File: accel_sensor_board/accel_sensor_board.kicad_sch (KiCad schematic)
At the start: 31 parts, among them J1 TagConnect_TC2030-NL, J2 USB_C_Receptacle_USB2.0_16P, SW1 SW_Push, U1 STM32F405RGT6, U2 USBLC6-2SC6, U3 TXB0106PW, U4 DIX9211PTR, X1 16MHz, X2 32kHz768

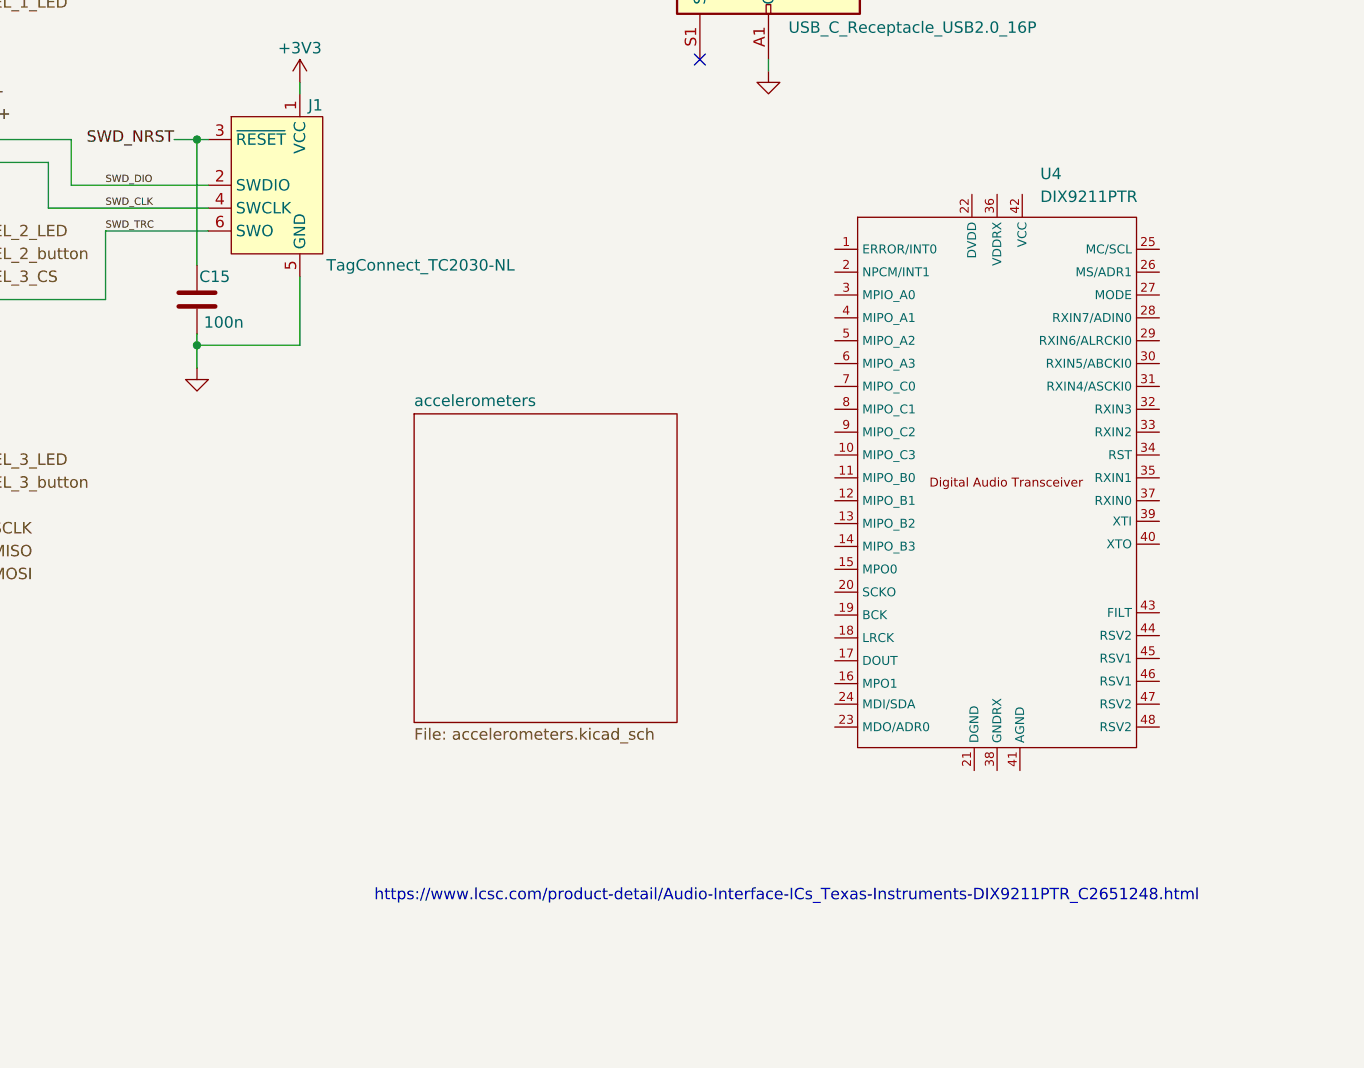
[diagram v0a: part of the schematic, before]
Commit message: added different audio driver / dac
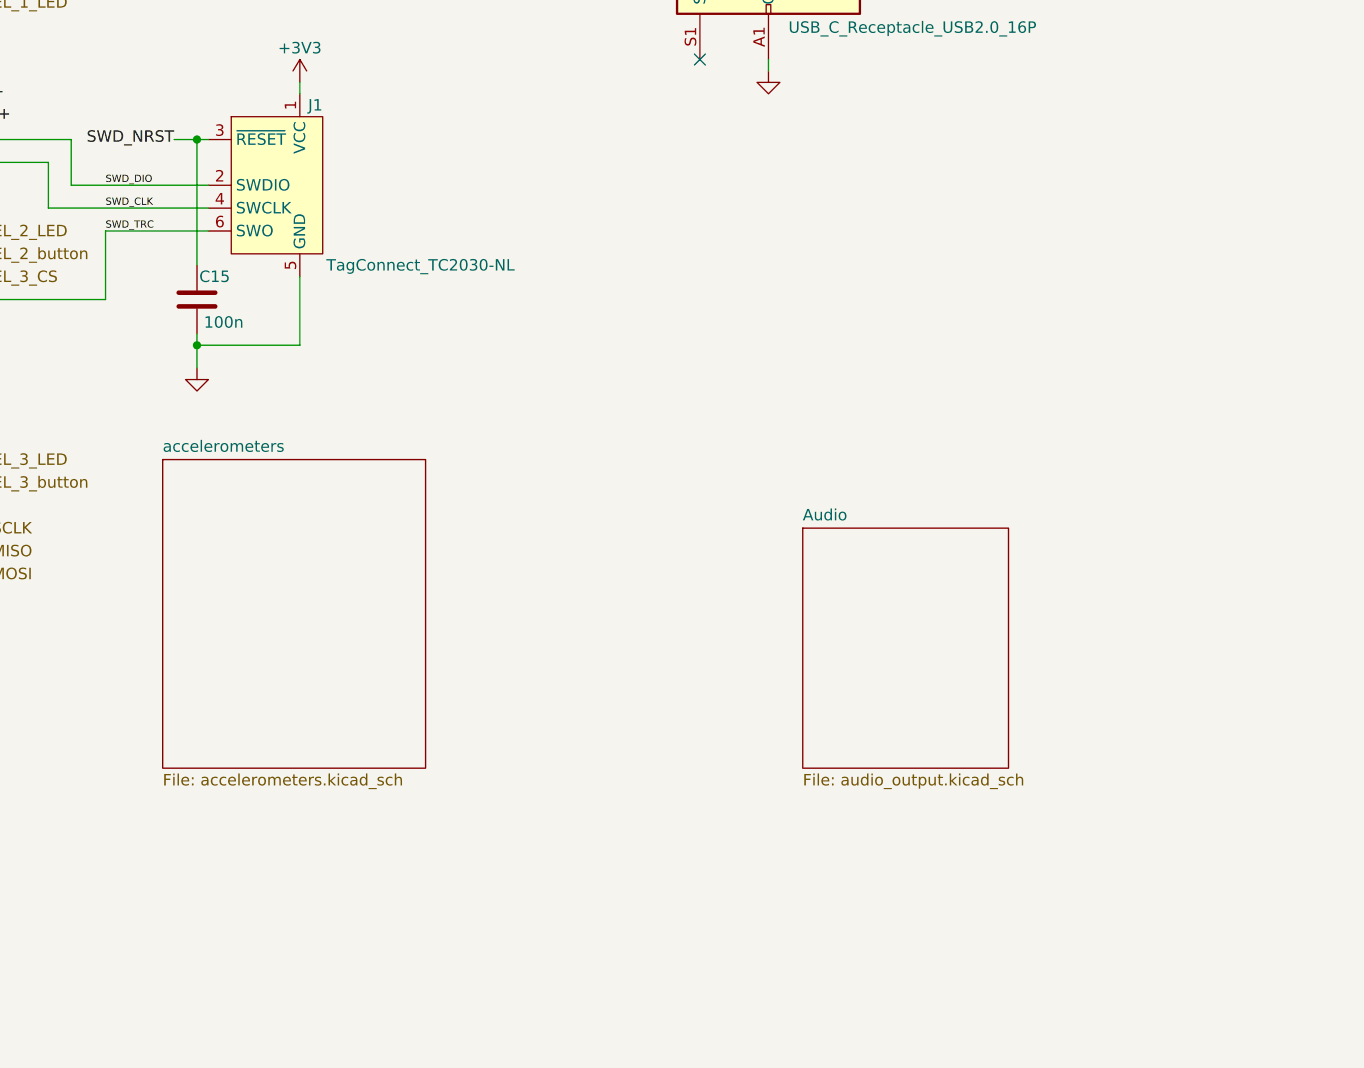
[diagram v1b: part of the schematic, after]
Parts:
- removed U4: DIX9211PTR, symbol Audio_DAC:DIX9211
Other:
- added sheet Audio (audio_output.kicad_sch)
- note removed: "https://www.lcsc.com/product-detail/Audio-Interface-ICs_Texas-Instruments-DIX9211PTR_C2651248.html"
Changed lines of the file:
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@@
 		)
 	)
-	(text "https://www.lcsc.com/product-detail/Audio-Interface-ICs_Texas-Instruments-DIX9211PTR_C2651248.html"
-		(exclude_from_sim no)
-		(at 229.362 160.274 0)
-		(effects
-			(font
-				(size 1.27 1.27)
-			)
-		)
-	)
 	(label "BOOT0"
 		(at 88.9 48.26 180)
@@
 	)
 	(symbol
-		(lib_id "Audio_DAC:DIX9211")
-		(at 252.73 114.3 0)
-		(unit 1)
-		(exclude_from_sim no)
-		(in_bom yes)
-		(on_board yes)
-		(dnp no)
-		(fields_autoplaced yes)
-		(property "Reference" "U4"
-			(at 257.5259 80.01 0)
-			(effects
-				(font
-					(size 1.27 1.27)
-				)
-				(justify left)
-			)
-		)
-		(property "Value" "DIX9211PTR"
-			(at 257.5259 82.55 0)
-			(effects
-				(font
-					(size 1.27 1.27)
-				)
-				(justify left)
-			)
-		)
-		(property "Footprint" ""
-			(at 252.73 114.3 0)
-			(effects
-				(font
-					(size 1.27 1.27)
-				)
-				(hide yes)
-			)
-		)
-		(property "Datasheet" "https://www.lcsc.com/datasheet/lcsc_datasheet_2302221130_Texas-Instruments-DIX9211PTR_C2651248.pdf"
-			(at 252.73 153.924 0)
-			(effects
-				(font
-					(size 1.27 1.27)
-				)
-				(hide yes)
-			)
-		)
-		(property "Description" "Digital Audio Interface Transceiver"
-			(at 252.73 156.718 0)
-			(effects
-				(font
-					(size 1.27 1.27)
-				)
-				(hide yes)
-			)
-		)
-		(pin "22"
-		)
-		(pin "37"
-		)
-		(pin "26"
-		)
-		(pin "11"
-		)
-		(pin "13"
-		)
-		(pin "40"
-		)
-		(pin "6"
-		)
-		(pin "24"
-		)
-		(pin "35"
-		)
-		(pin "8"
-		)
-		(pin "34"
-		)
-		(pin "27"
-		)
-		(pin "31"
-		)
-		(pin "29"
-		)
-		(pin "32"
-		)
-		(pin "23"
-		)
-		(pin "19"
-		)
-		(pin "3"
-		)
-		(pin "38"
-		)
-		(pin "25"
-		)
-		(pin "42"
-		)
-		(pin "18"
-		)
-		(pin "9"
-		)
-		(pin "14"
-		)
-		(pin "2"
-		)
-		(pin "21"
-		)
-		(pin "10"
-		)
-		(pin "4"
-		)
-		(pin "43"
-		)
-		(pin "33"
-		)
-		(pin "45"
-		)
-		(pin "30"
-		)
-		(pin "12"
-		)
-		(pin "20"
-		)
-		(pin "39"
-		)
-		(pin "28"
-		)
-		(pin "41"
-		)
-		(pin "46"
-		)
-		(pin "47"
-		)
-		(pin "48"
-		)
-		(pin "36"
-		)
-		(pin "44"
-		)
-		(pin "16"
-		)
-		(pin "5"
-		)
-		(pin "17"
-		)
-		(pin "1"
-		)
-		(pin "15"
-		)
-		(pin "7"
-		)
-		(instances
-			(project ""
-				(path "/0dfa5a60-fde1-46af-b0d4-ff3239ee4fa1"
-					(reference "U4")
-					(unit 1)
-				)
-			)
-		)
-	)
-	(symbol
 		(lib_id "Device:R")
 		(at 114.3 175.26 0)
@@
 	)
 	(sheet
-		(at 187.96 106.68)
+		(at 160.02 111.76)
 		(size 29.21 34.29)
 		(fields_autoplaced yes)
@@
 		)
 		(property "Sheetname" "accelerometers"
-			(at 187.96 105.9684 0)
+			(at 160.02 111.0484 0)
 			(effects
 				(font
@@
 		)
 		(property "Sheetfile" "accelerometers.kicad_sch"
-			(at 187.96 141.5546 0)
+			(at 160.02 146.6346 0)
 			(effects
 				(font
@@
 				)
 			)
+		)
+	)
+	(sheet
+		(at 231.14 119.38)
+		(size 22.86 26.67)
+		(fields_autoplaced yes)
+		(stroke
+			(width 0.1524)
+			(type solid)
+		)
+		(fill
+			(color 0 0 0 0.0000)
+		)
+		(property "Sheetname" "Audio"
+			(at 231.14 118.6684 0)
+			(effects
+				(font
+					(size 1.27 1.27)
+				)
+				(justify left bottom)
+			)
+		)
+		(property "Sheetfile" "audio_output.kicad_sch"
+			(at 231.14 146.6346 0)
+			(effects
+				(font
+					(size 1.27 1.27)
+				)
+				(justify left top)
+			)
+		)
+		(instances
+			(project "accel_sensor_board"
+				(path "/0dfa5a60-fde1-46af-b0d4-ff3239ee4fa1"
+					(page "3")
+				)
+			)

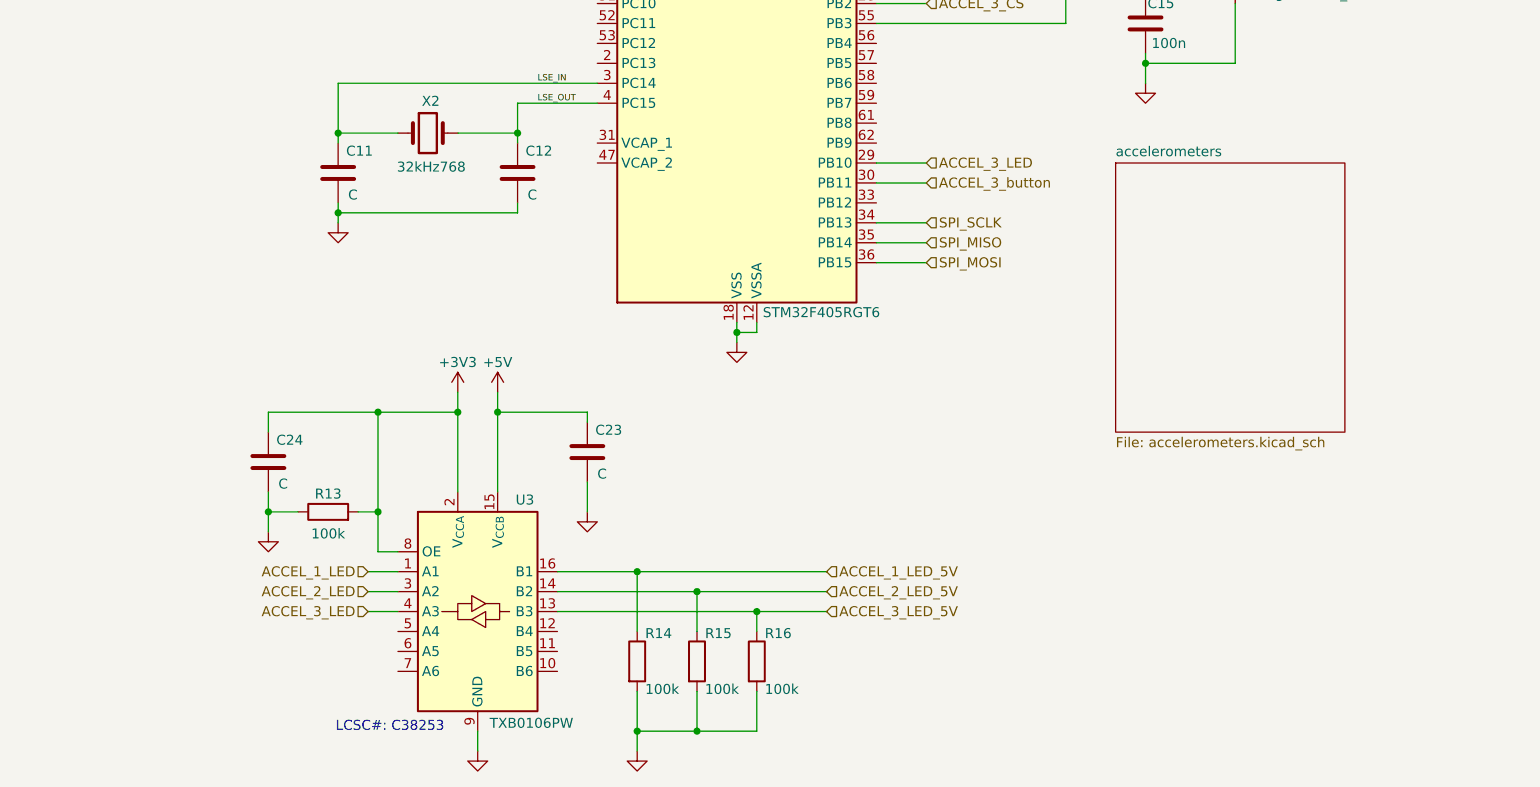
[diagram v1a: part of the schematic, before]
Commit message: updated accel labels
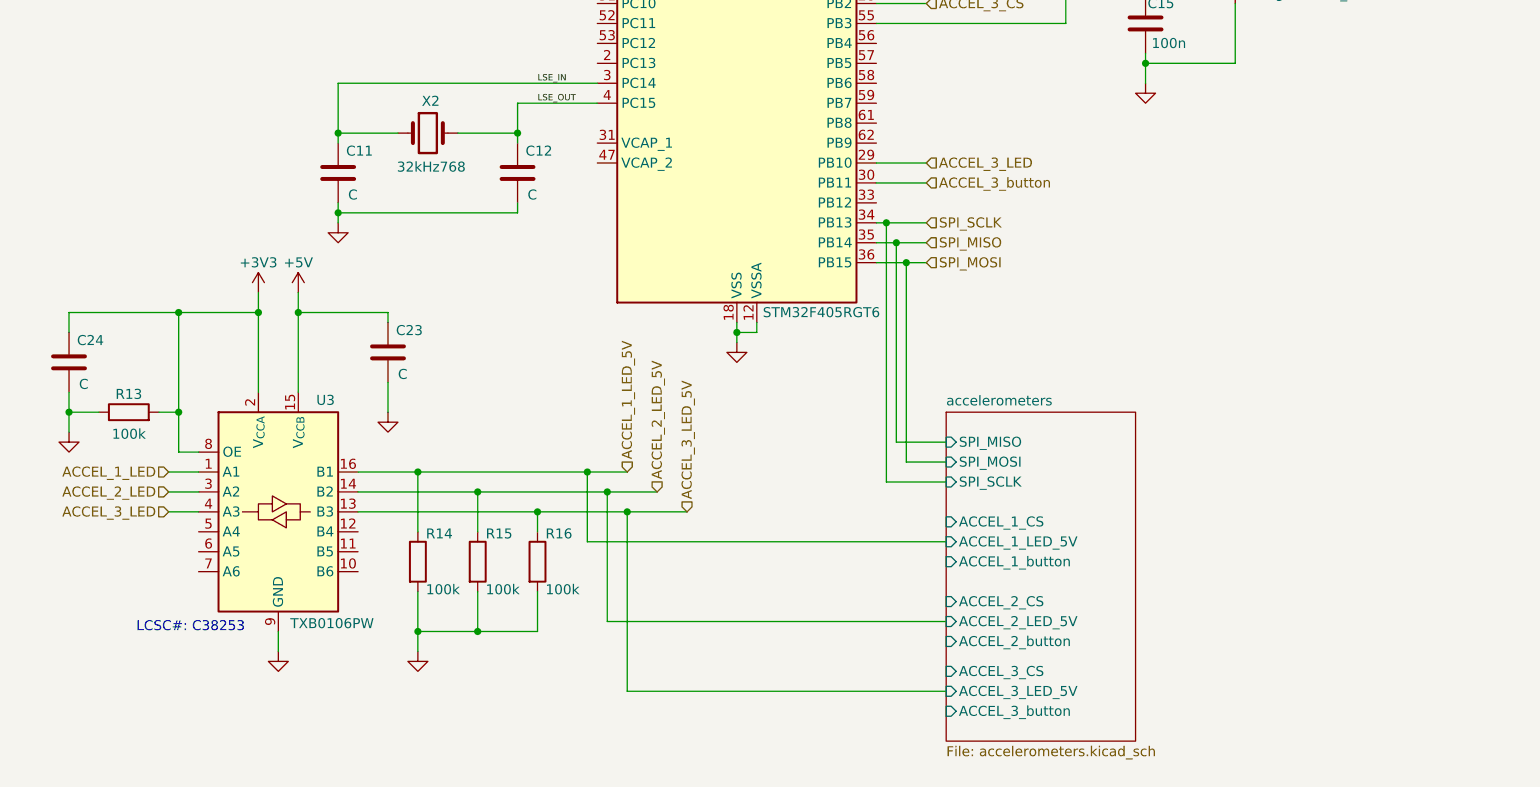
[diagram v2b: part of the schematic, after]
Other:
- sheet accelerometers ports: added ACCEL_1_CS, ACCEL_1_LED_5V, ACCEL_1_button, ACCEL_2_CS, ACCEL_2_LED_5V, ACCEL_2_button, ACCEL_3_CS, ACCEL_3_LED_5V, ACCEL_3_button, SPI_MISO, SPI_MOSI, SPI_SCLK; removed none
- moved on the sheet: C23, C24, R13, R14, R15, R16, U3
